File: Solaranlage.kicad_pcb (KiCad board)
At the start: 2 copper layers, 160 x 85 mm, 77 parts, among them J1 Screw_Terminal_01x02, J10 Conn_01x01_Male, J2 Screw_Terminal_01x02, J3 AVR-JTAG-10, J4 USB_B, J5 USB_B, J6 Screw_Terminal_01x02, J7 Conn_01x02_Male, J8 Conn_01x01_Male, J9 Conn_01x02_Male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

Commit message: ... and applied to layout
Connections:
- C11 pad 1: /AREF -> +5V
- U7 pad 32: /AREF -> +5V
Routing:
- net +5V: track 23.6 -> 36.9 mm
- net /AREF: track 13.3 -> 0.00 mm

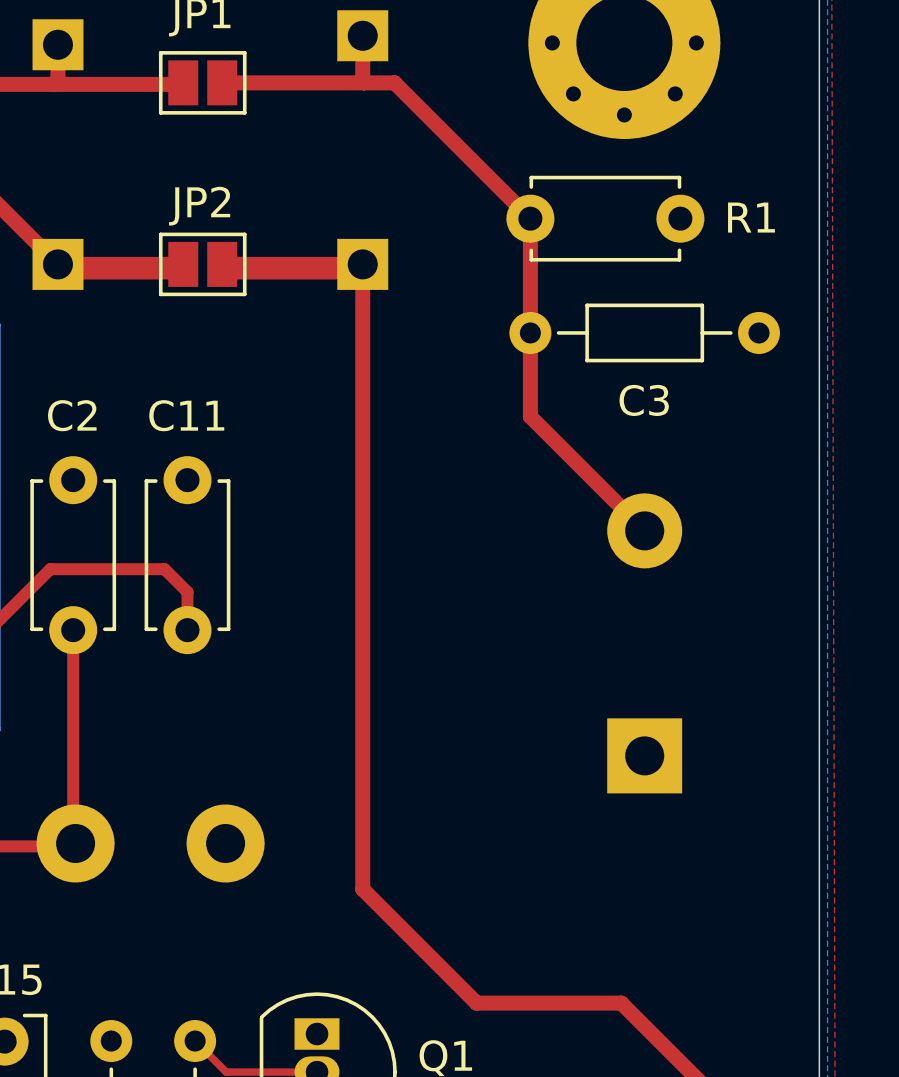
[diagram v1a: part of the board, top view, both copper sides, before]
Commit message: flipped designator C3 and R1 in silk screen
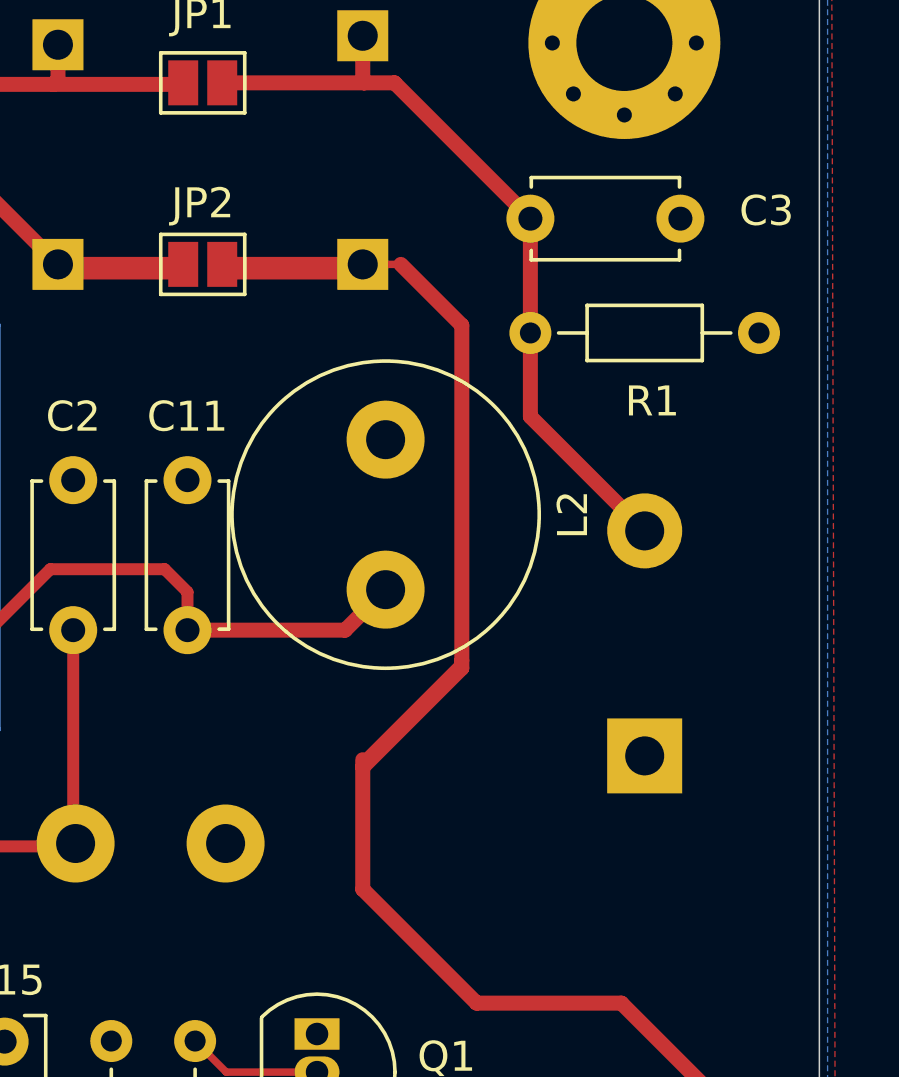
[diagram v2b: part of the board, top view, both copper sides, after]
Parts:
- added L2: INDUCTOR, Inductor_THT:L_Radial_D10.0mm_P5.00mm_Fastron_07P, F.Cu at (214.6, 74.9)
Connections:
- C11 pad 1: +5V -> /AREF
- U7 pad 32: +5V -> /AREF
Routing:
- net /AREF: track 0.00 -> 20.5 mm
- net +5V: track 36.9 -> 23.6 mm
- net Net-(C4-Pad1): track 58.4 -> 67.0 mm

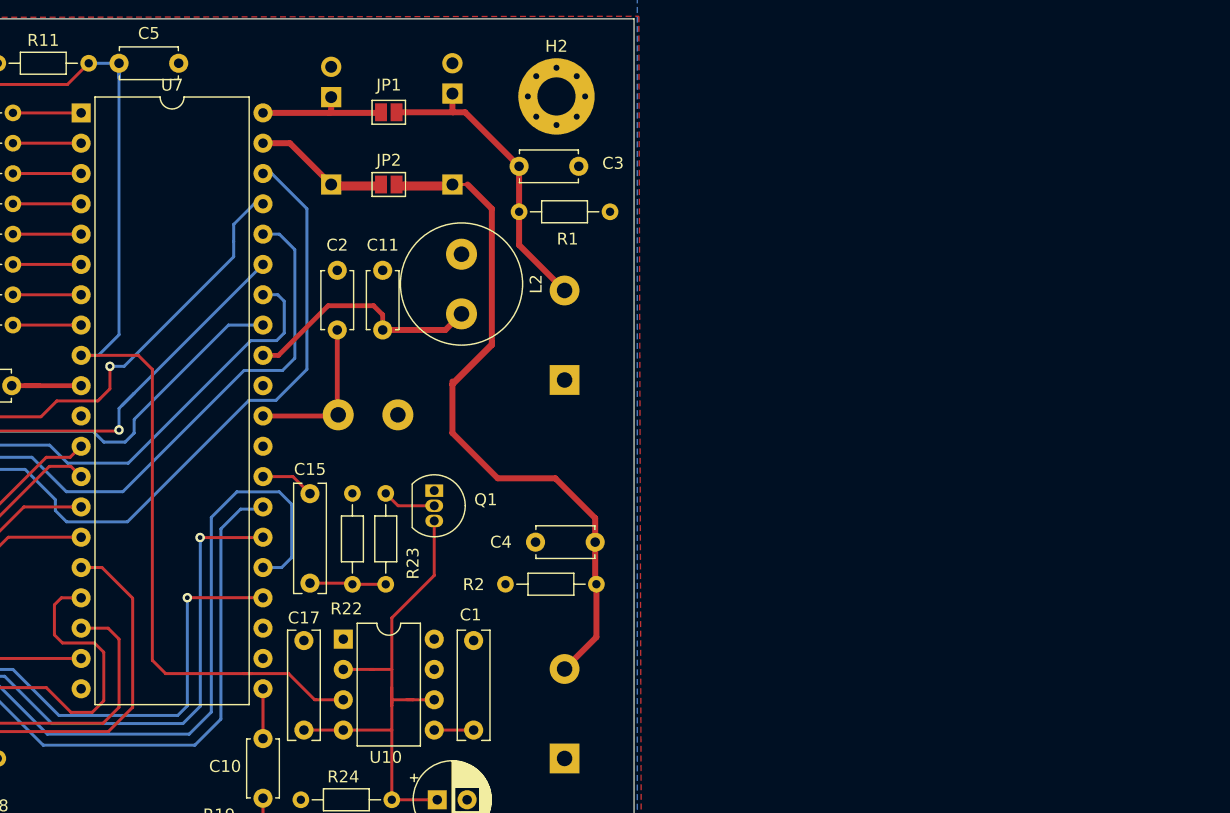
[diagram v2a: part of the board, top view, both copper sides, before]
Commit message: changed MCU from atmega32 to atmega644 because of availability;added 12p->GND to TCK to make JTAG working
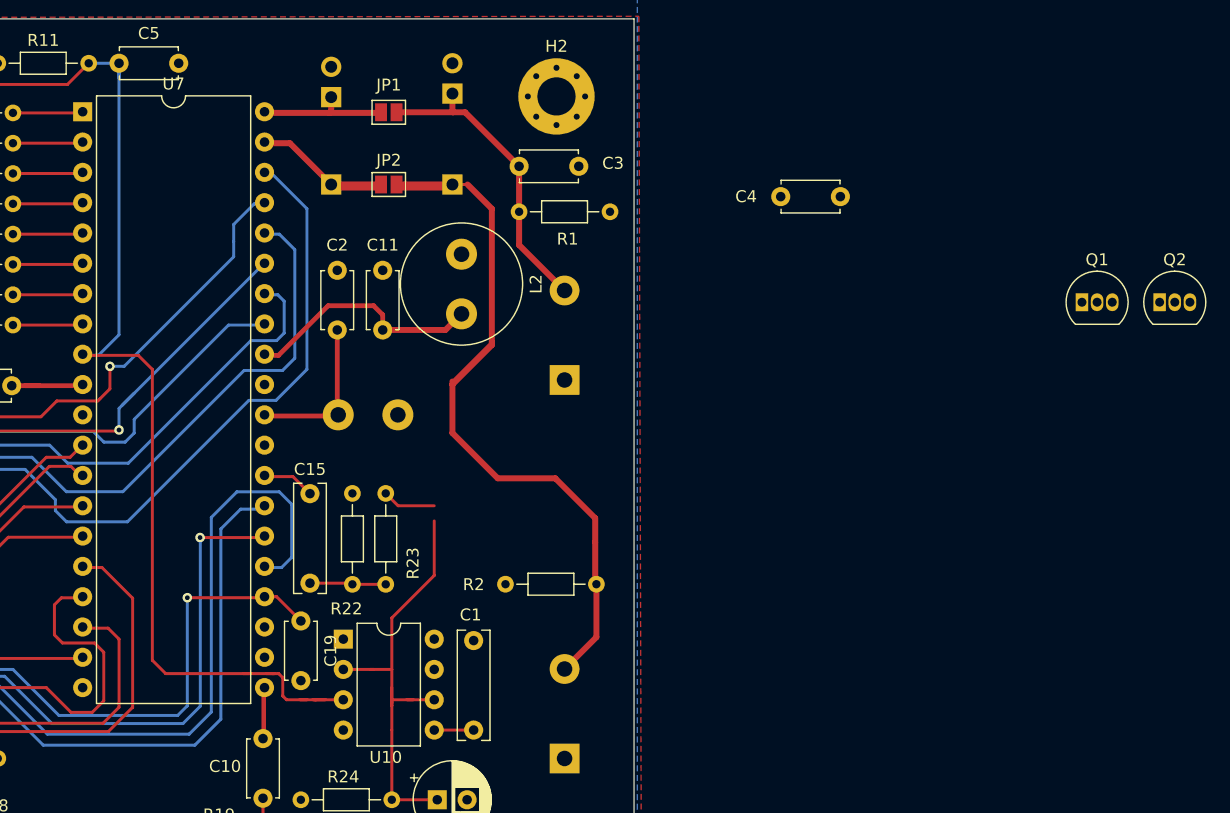
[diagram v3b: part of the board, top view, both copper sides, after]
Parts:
- removed C17: 10n, Capacitor_THT:C_Rect_L9.0mm_W2.5mm_P7.50mm_MKT
- added C19: 10p, Capacitor_THT:C_Disc_D4.7mm_W2.5mm_P5.00mm, F.Cu at (201.2, 105.7)
- added Q2: BC328, Package_TO_SOT_THT:TO-92_Inline, F.Cu at (273.1, 79.0)
- C12, C13: value 100n -> 10p
- Q1: value 2N7000 -> 2N3904
- U7: value ATmega32-16PU -> ATmega644-20PU
- moved Q1 56.5 mm to (266.6, 79.0), turned to 0 degrees
- moved C4 35.5 mm to (246.4, 70.1)
- moved U7 0.16 mm to (182.9, 63.0)
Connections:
- U10 pad 4: Net-(C16-Pad1) -> +5V
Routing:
- net Net-(C16-Pad1): track 45.9 -> 38.6 mm
- net /PWM: track 4.68 -> 9.01 mm
- net TCK: track 158.4 -> 162.3 mm
- net \RST: track 196.8 -> 200.3 mm

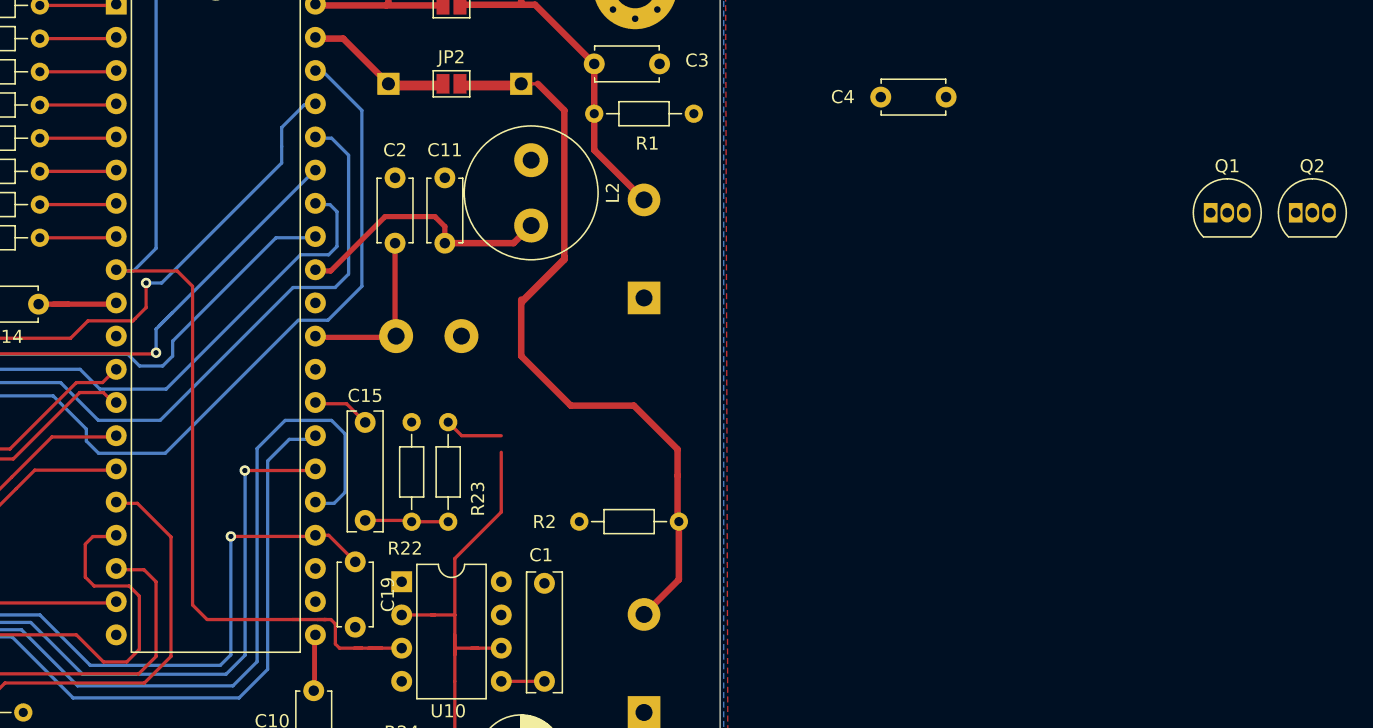
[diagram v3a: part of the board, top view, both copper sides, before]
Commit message: added Q2 to watchdog circuit;
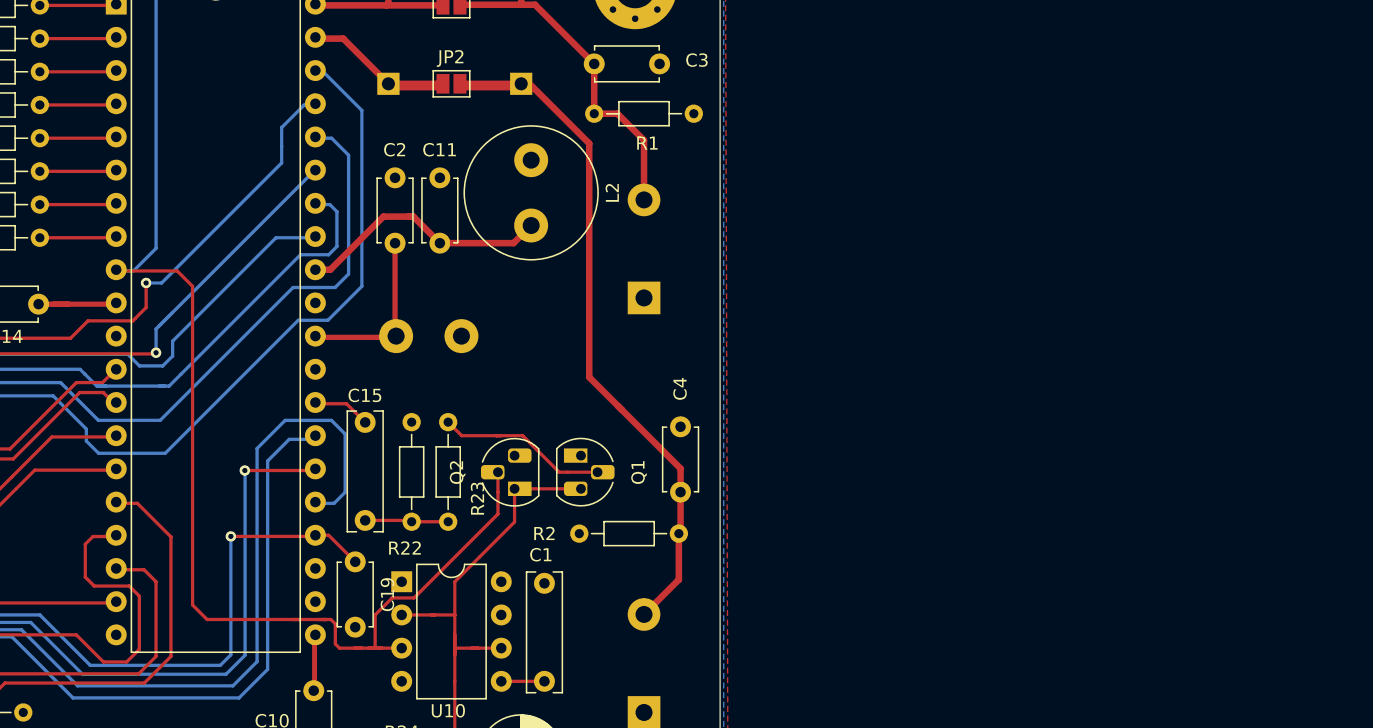
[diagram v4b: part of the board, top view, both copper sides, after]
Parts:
- Q1, Q2: footprint Package_TO_SOT_THT:TO-92_Inline -> Package_TO_SOT_THT:TO-92_HandSolder
- moved Q2 63.4 mm to (213.4, 100.1), turned to 90 degrees
- moved Q1 51.6 mm to (218.4, 97.5), turned to 270 degrees
- moved C4 36.4 mm to (226.1, 100.3), turned to 90 degrees
- moved R2 0.92 mm to (218.3, 103.5)
- moved C11 0.38 mm to (207.6, 81.3)
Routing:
- net \RST: track 200.3 -> 218.6 mm
- net Net-(C4-Pad1): track 67.0 -> 56.7 mm
- net Net-(Q1-Pad2): track 4.49 -> 13.4 mm
- net Net-(C16-Pad1): track 38.6 -> 41.3 mm
- net Net-(C3-Pad1): track 25.7 -> 26.8 mm
- net /AREF: track 20.5 -> 19.6 mm
- net /DZ: track 106.1 -> 106.9 mm

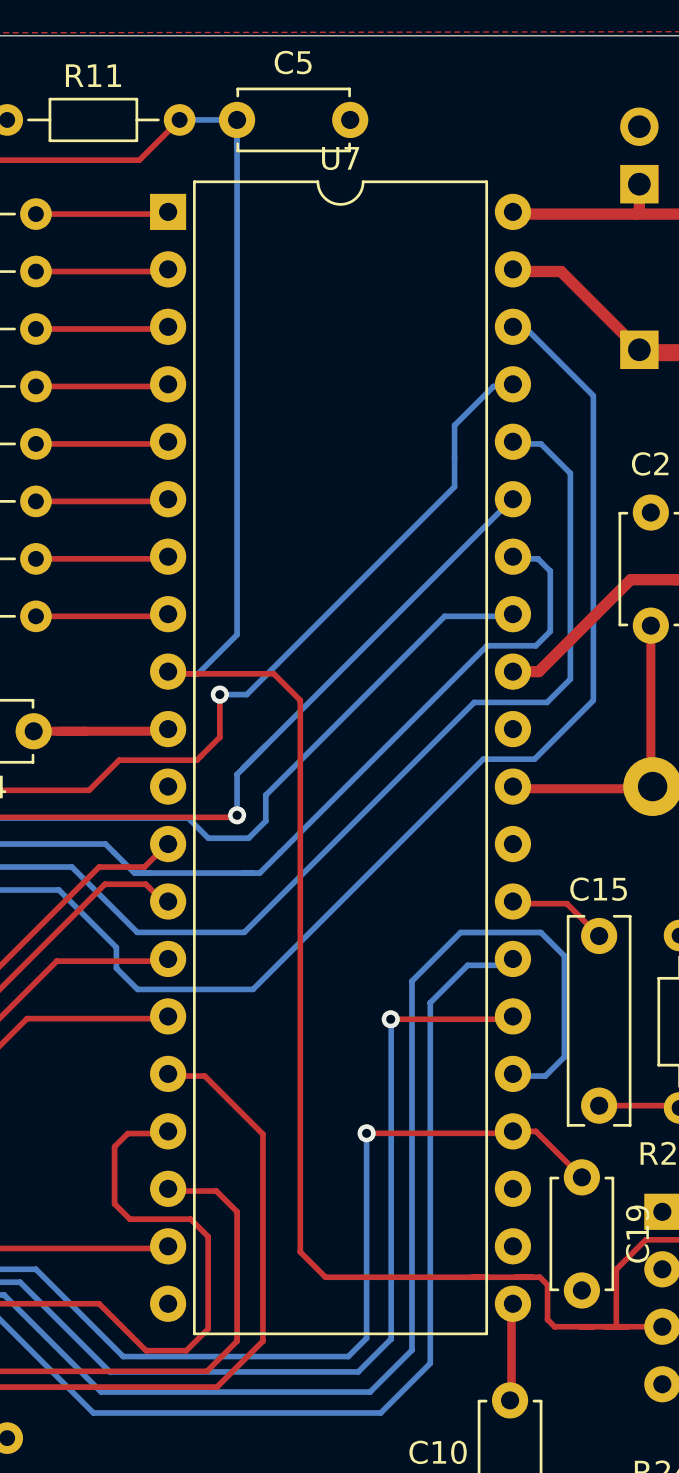
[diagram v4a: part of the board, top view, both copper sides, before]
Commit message: changed MCU back to atmega32
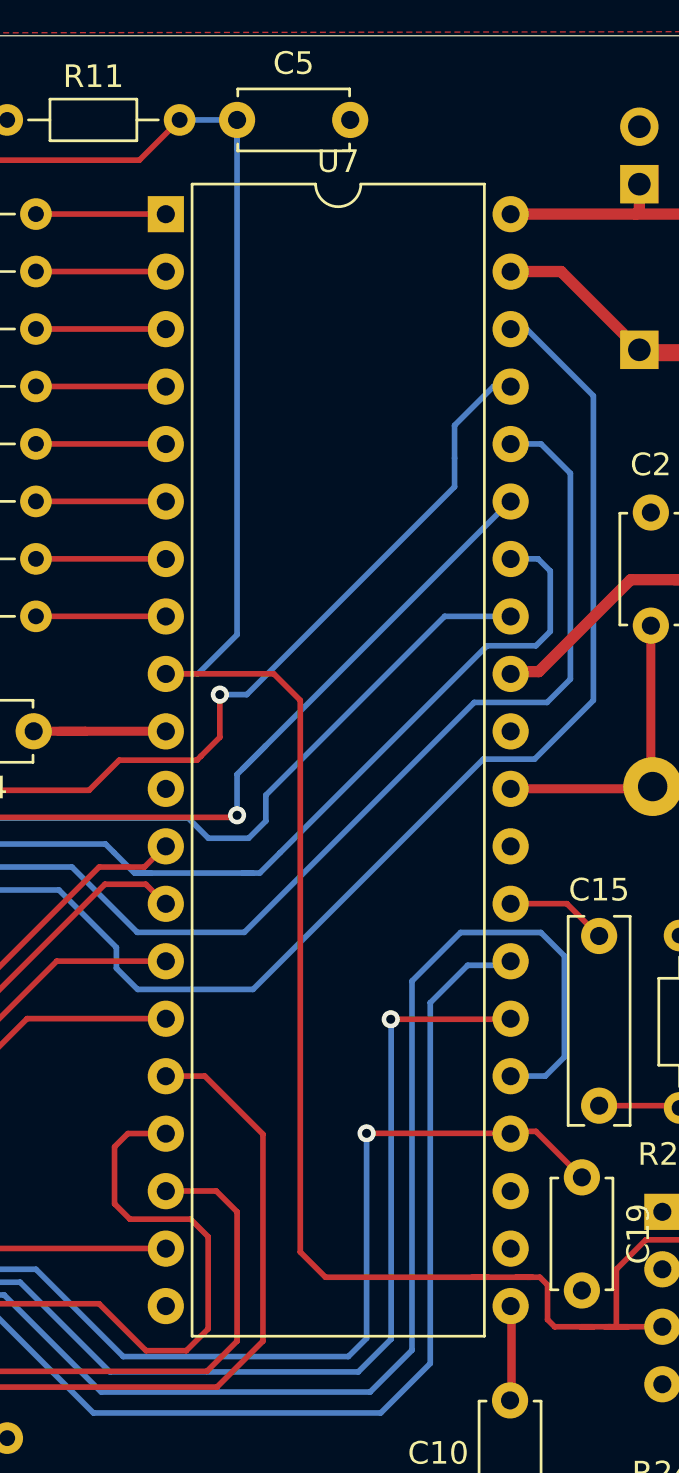
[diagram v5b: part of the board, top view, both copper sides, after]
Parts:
- U7: value ATmega644-20PU -> ATmega32-16PU
- moved U7 0.14 mm to (182.8, 63.1)
